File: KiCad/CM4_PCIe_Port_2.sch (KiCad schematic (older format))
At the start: 1 part, among them J13 PCIe_x16

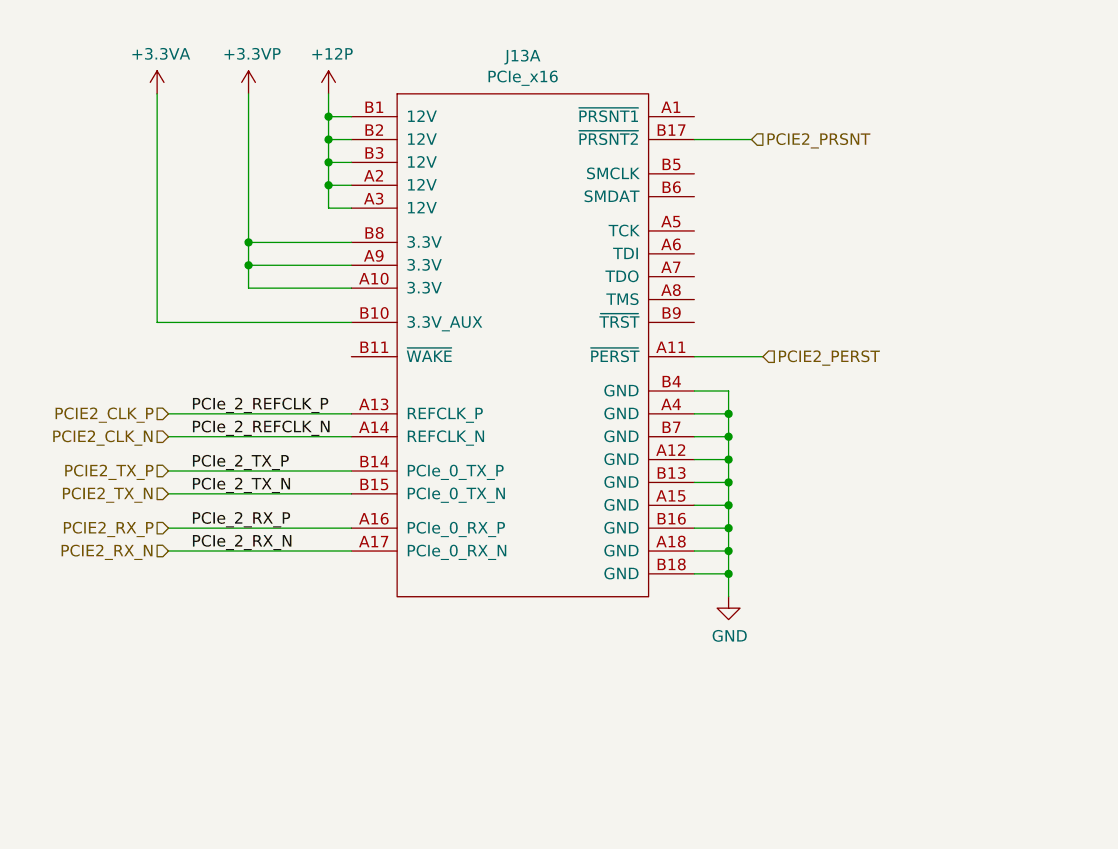
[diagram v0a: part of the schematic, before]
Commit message: Adding PCIe subsystem
- Moves a lot of the PCIe related items from the top level sheet to a new sheet called PCIe Subsystem which then has other hierarchical sheets below it.

- This adds some of the AC coupling caps for the PCIe slots, might need to do some work with the switch yet.

- Adds an SMBUS mux for the SMBUS connections to the PCIe slots. Extra SMBUS lanes sit un-wired and can be used for other things.

- Adds JTAG headers for the PCIe connectors.
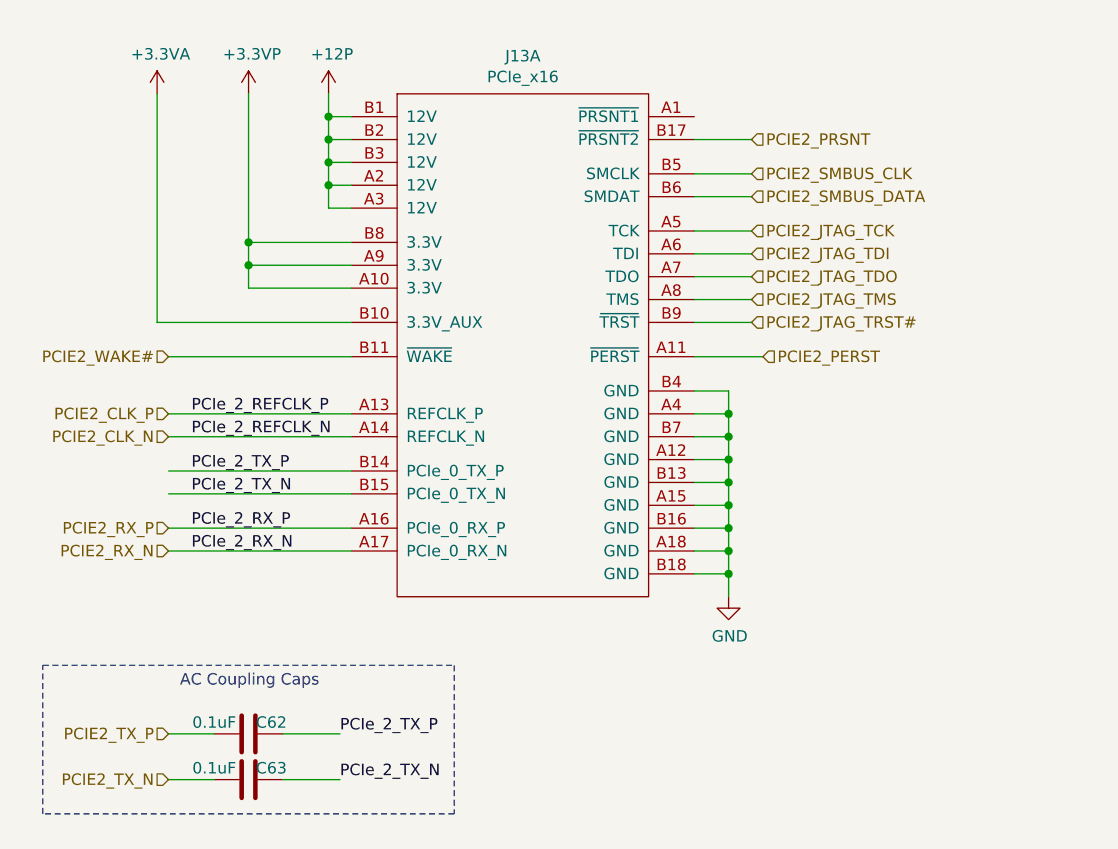
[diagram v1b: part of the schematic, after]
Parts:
- added C62, C63: 0.1uF, symbol CM4_MATX:C
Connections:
- net PCIE2_TX_N: now also C63.2; no longer J13.B15 (PCIe_0_TX_N)
- net PCIE2_TX_P: now also C62.1; no longer J13.B14 (PCIe_0_TX_P)
- net PCIE2_JTAG_TCK: now reaches J13.A5 (TCK)
- net PCIE2_JTAG_TDI: now reaches J13.A6 (TDI)
- net PCIE2_JTAG_TDO: now reaches J13.A7 (TDO)
- net PCIE2_JTAG_TMS: now reaches J13.A8 (TMS)
- net PCIE2_WAKE#: now reaches J13.B11 (~WAKE)
- net PCIE2_SMBUS_CLK: now reaches J13.B5 (SMCLK)
- net PCIE2_SMBUS_DATA: now reaches J13.B6 (SMDAT)
- net PCIE2_JTAG_TRST#: now reaches J13.B9 (~TRST)
- new net PCIe_2_TX_N: C63.1, J13.B15 (PCIe_0_TX_N)
- new net PCIe_2_TX_P: C62.2, J13.B14 (PCIe_0_TX_P)
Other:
- note added: "AC Coupling Caps"
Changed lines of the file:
@@
 $Descr A4 11693 8268
 encoding utf-8
-Sheet 7 12
+Sheet 11 15
 Title "PCIe x16 - Slot 2"
 Date "2020-12-28"
@@
 Text HLabel 1450 4550 0    50   Input ~ 0
 PCIE2_RX_N
-Text HLabel 1450 4300 0    50   Input ~ 0
+Text HLabel 1450 5550 0    50   Input ~ 0
 PCIE2_TX_N
-Text HLabel 1450 4200 0    50   Input ~ 0
+Text HLabel 1450 5350 0    50   Input ~ 0
 PCIE2_TX_P
 $Comp
@@
 AR Path="/5FCA7683/5FEA62ED" Ref="#PWR?"  Part="1"
 AR Path="/5FD73012/5FEA62ED" Ref="#PWR0135"  Part="1"
-F 0 "#PWR0135" H 3900 4500 50  0001 C CNN
+AR Path="/5FFBC089/5FFBFF20/5FEA62ED" Ref="#PWR0151"  Part="1"
+F 0 "#PWR0151" H 3900 4500 50  0001 C CNN
 F 1 "GND" H 3905 4577 50  0000 C CNN
 F 2 "" H 3900 4750 50  0001 C CNN
@@
 AR Path="/5FCA7683/5FEA6319" Ref="#PWR?"  Part="1"
 AR Path="/5FD73012/5FEA6319" Ref="#PWR0139"  Part="1"
-F 0 "#PWR0139" H 2150 2400 50  0001 C CNN
+AR Path="/5FFBC089/5FFBFF20/5FEA6319" Ref="#PWR0152"  Part="1"
+F 0 "#PWR0152" H 2150 2400 50  0001 C CNN
 F 1 "+12P" H 2165 2723 50  0000 C CNN
 F 2 "" H 2150 2550 50  0001 C CNN
@@
 AR Path="/5FCA7683/5FEA632D" Ref="#PWR?"  Part="1"
 AR Path="/5FD73012/5FEA632D" Ref="#PWR0140"  Part="1"
-F 0 "#PWR0140" H 1950 2500 50  0001 C CNN
+AR Path="/5FFBC089/5FFBFF20/5FEA632D" Ref="#PWR0184"  Part="1"
+F 0 "#PWR0184" H 1950 2500 50  0001 C CNN
 F 1 "+3.3VP" H 1815 2723 50  0000 C CNN
 F 2 "" H 1800 2550 50  0001 C CNN
@@
 AR Path="/5FCA7683/5FEA633B" Ref="#PWR?"  Part="1"
 AR Path="/5FD73012/5FEA633B" Ref="#PWR0141"  Part="1"
-F 0 "#PWR0141" H 1400 2400 50  0001 C CNN
+AR Path="/5FFBC089/5FFBFF20/5FEA633B" Ref="#PWR0185"  Part="1"
+F 0 "#PWR0185" H 1400 2400 50  0001 C CNN
 F 1 "+3.3VA" H 1415 2723 50  0000 C CNN
 F 2 "" H 1400 2550 50  0001 C CNN
@@
 U 1 1 5FED8C9C
 P 3050 4400
+AR Path="/5FD73012/5FED8C9C" Ref="J13"  Part="1"
+AR Path="/5FFBC089/5FFBFF20/5FED8C9C" Ref="J13"  Part="1"
 F 0 "J13" H 3000 6415 50  0000 C CNN
 F 1 "PCIe_x16" H 3000 6324 50  0000 C CNN
@@
 U 2 1 5FEDF22E
 P 8150 3900
+AR Path="/5FD73012/5FEDF22E" Ref="J13"  Part="2"
+AR Path="/5FFBC089/5FFBFF20/5FEDF22E" Ref="J13"  Part="2"
 F 0 "J13" H 8150 5915 50  0000 C CNN
 F 1 "PCIe_x16" H 8150 5824 50  0000 C CNN
@@
 U 3 1 5FEE2CC4
 P 9950 3450
+AR Path="/5FD73012/5FEE2CC4" Ref="J13"  Part="3"
+AR Path="/5FFBC089/5FFBFF20/5FEE2CC4" Ref="J13"  Part="3"
 F 0 "J13" H 9950 5465 50  0000 C CNN
 F 1 "PCIe_x16" H 9950 5374 50  0000 C CNN
@@
 U 1 1 600B9F64
 P 10800 5450
-F 0 "#PWR0189" H 10800 5200 50  0001 C CNN
+AR Path="/5FD73012/600B9F64" Ref="#PWR0189"  Part="1"
+AR Path="/5FFBC089/5FFBFF20/600B9F64" Ref="#PWR0186"  Part="1"
+F 0 "#PWR0186" H 10800 5200 50  0001 C CNN
 F 1 "GND" H 10805 5277 50  0000 C CNN
 F 2 "" H 10800 5450 50  0001 C CNN
@@
 U 1 1 600BA254
 P 9000 5550
-F 0 "#PWR0190" H 9000 5300 50  0001 C CNN
+AR Path="/5FD73012/600BA254" Ref="#PWR0190"  Part="1"
+AR Path="/5FFBC089/5FFBFF20/600BA254" Ref="#PWR0187"  Part="1"
+F 0 "#PWR0187" H 9000 5300 50  0001 C CNN
 F 1 "GND" H 9005 5377 50  0000 C CNN
 F 2 "" H 9000 5550 50  0001 C CNN
@@
 	1    0    0    -1
 $EndComp
+Wire Wire Line
+	1450 5550 1650 5550
+Wire Wire Line
+	1450 5350 1650 5350
+$Comp
+L CM4_MATX:C C?
+U 1 1 5FF242AA
+P 1800 5550
+AR Path="/5FCA7683/5FF242AA" Ref="C?"  Part="1"
+AR Path="/5FFBC089/5FFBFF20/5FF242AA" Ref="C63"  Part="1"
+F 0 "C63" V 1750 5650 50  0000 C CNN
+F 1 "0.1uF" V 1750 5400 50  0000 C CNN
+F 2 "" H 1838 5400 50  0001 C CNN
+F 3 "~" H 1800 5550 50  0001 C CNN
+	1    1800 5550
+	0    1    1    0
+$EndComp
+$Comp
+L CM4_MATX:C C?
+U 1 1 5FF242B0
+P 1800 5350
+AR Path="/5FCA7683/5FF242B0" Ref="C?"  Part="1"
+AR Path="/5FFBC089/5FFBFF20/5FF242B0" Ref="C62"  Part="1"
+F 0 "C62" V 1850 5250 50  0000 C CNN
+F 1 "0.1uF" V 1850 5500 50  0000 C CNN
+F 2 "" H 1838 5200 50  0001 C CNN
+F 3 "~" H 1800 5350 50  0001 C CNN
+	1    1800 5350
+	0    -1   -1   0
+$EndComp
+Wire Wire Line
+	1950 5550 2200 5550
+Wire Wire Line
+	1950 5350 2200 5350
+Text Notes 1500 5150 0    50   ~ 0
+AC Coupling Caps
+Wire Notes Line
+	900  5050 2700 5050
+Wire Notes Line
+	2700 5050 2700 5700
+Wire Notes Line
+	2700 5700 900  5700
+Wire Notes Line
+	900  5700 900  5050
+Text Label 2200 5350 0    50   ~ 0
+PCIe_2_TX_P
+Text Label 2200 5550 0    50   ~ 0
+PCIe_2_TX_N
+Wire Wire Line
+	3750 2900 4000 2900
+Wire Wire Line
+	3750 3000 4000 3000
+Text HLabel 4000 2900 2    50   Input ~ 0
+PCIE2_SMBUS_CLK
+Text HLabel 4000 3000 2    50   Input ~ 0
+PCIE2_SMBUS_DATA
+Wire Wire Line
+	2250 3700 1450 3700
+Text HLabel 1450 3700 0    50   Input ~ 0
+PCIE2_WAKE#
+Wire Wire Line
+	3750 3150 4000 3150
+Wire Wire Line
+	3750 3250 4000 3250
+Wire Wire Line
+	3750 3350 4000 3350
+Wire Wire Line
+	3750 3450 4000 3450
+Wire Wire Line
+	3750 3550 4000 3550
+Text HLabel 4000 3150 2    50   Input ~ 0
+PCIE2_JTAG_TCK
+Text HLabel 4000 3250 2    50   Input ~ 0
+PCIE2_JTAG_TDI
+Text HLabel 4000 3350 2    50   Input ~ 0
+PCIE2_JTAG_TDO
+Text HLabel 4000 3450 2    50   Input ~ 0
+PCIE2_JTAG_TMS
+Text HLabel 4000 3550 2    50   Input ~ 0
+PCIE2_JTAG_TRST#
 $EndSCHEMATC
